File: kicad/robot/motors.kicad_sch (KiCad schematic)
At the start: 15 parts, among them J3 67996-412HLF, Q6 SN74AHC125RGYR, U8 DRV8830DRCR, U9 DRV8830DRCR

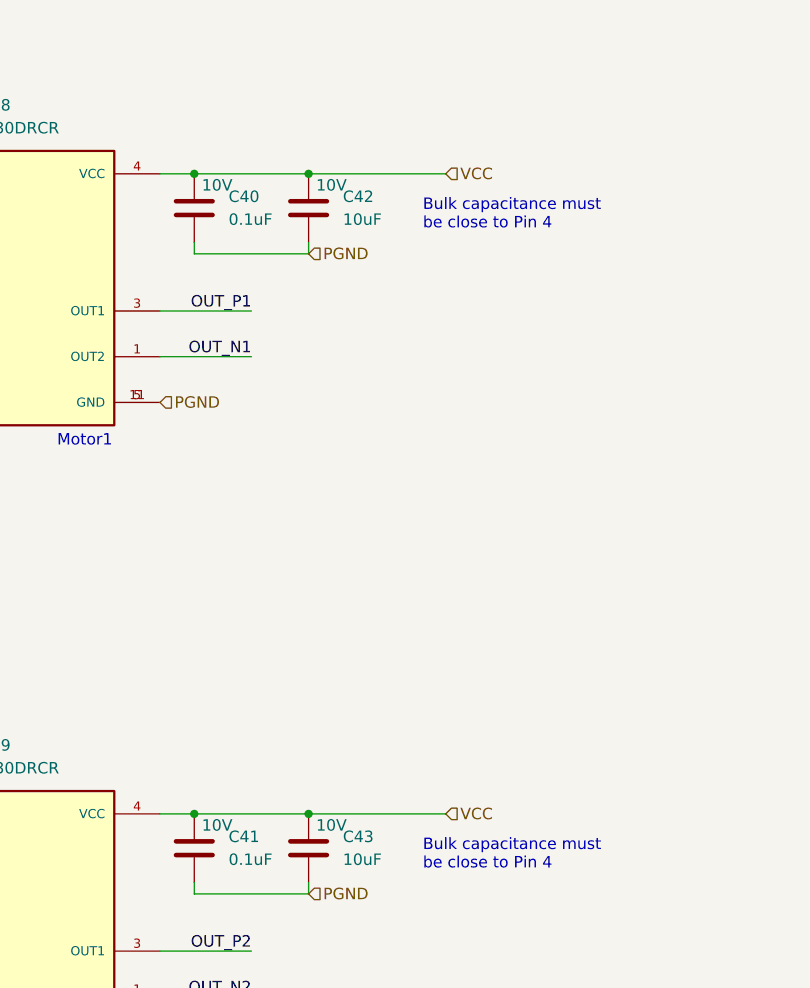
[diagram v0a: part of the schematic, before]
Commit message: Add current breaks between each section of hardware.
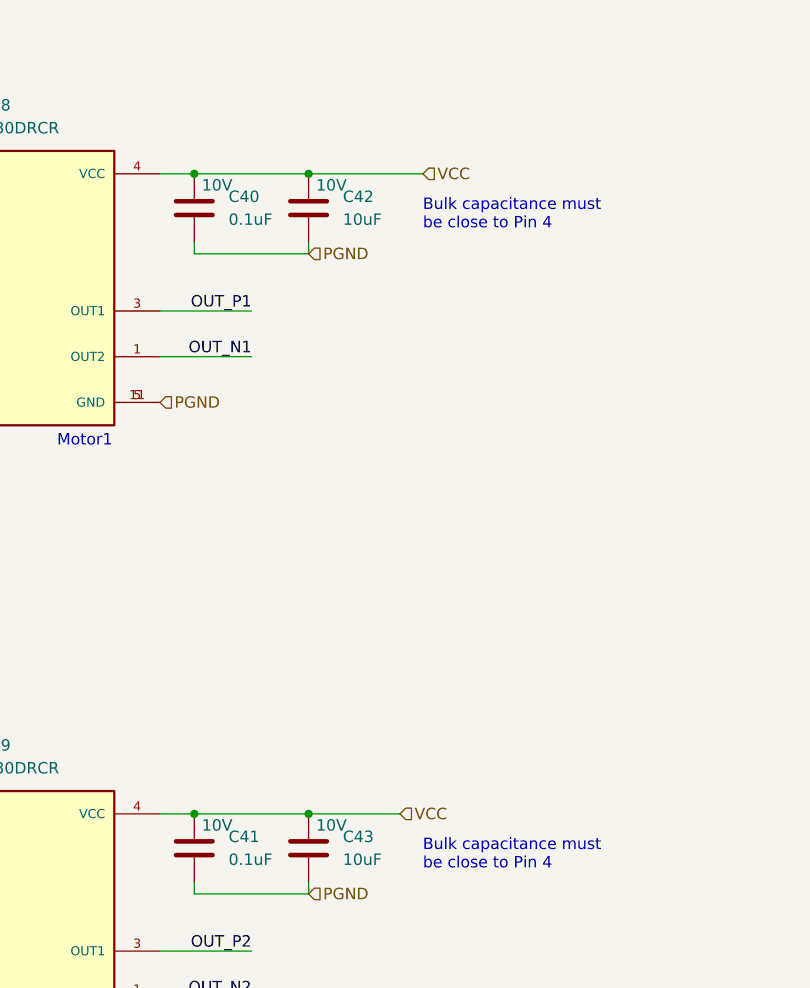
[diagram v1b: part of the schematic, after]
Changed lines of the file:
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@@
     (stroke (width 0) (type default))
   )
-  (wire (pts (xy 146.05 116.84) (xy 130.81 116.84))
+  (wire (pts (xy 140.97 116.84) (xy 130.81 116.84))
     (stroke (width 0) (type default))
   )
@@
     (stroke (width 0) (type default))
   )
-  (wire (pts (xy 146.05 45.72) (xy 130.81 45.72))
+  (wire (pts (xy 130.81 45.72) (xy 143.51 45.72))
     (stroke (width 0) (type default))
   )
@@
     (effects (font (size 1.27 1.27)) (justify left bottom))
   )
-  (hierarchical_label "VCC" (shape input) (at 146.05 45.72 0) (fields_autoplaced)
+  (hierarchical_label "VCC" (shape input) (at 143.51 45.72 0) (fields_autoplaced)
     (effects (font (size 1.27 1.27)) (justify left))
   )
@@
     (effects (font (size 1.27 1.27)) (justify right))
   )
-  (hierarchical_label "VCC" (shape input) (at 146.05 116.84 0) (fields_autoplaced)
-    (effects (font (size 1.27 1.27)) (justify left))
-  )
   (hierarchical_label "VIO" (shape input) (at 73.66 105.41 0) (fields_autoplaced)
     (effects (font (size 1.27 1.27)) (justify left))
@@
     (effects (font (size 1.27 1.27)) (justify left))
   )
+  (hierarchical_label "VCC" (shape input) (at 140.97 116.84 0) (fields_autoplaced)
+    (effects (font (size 1.27 1.27)) (justify left))
+  )

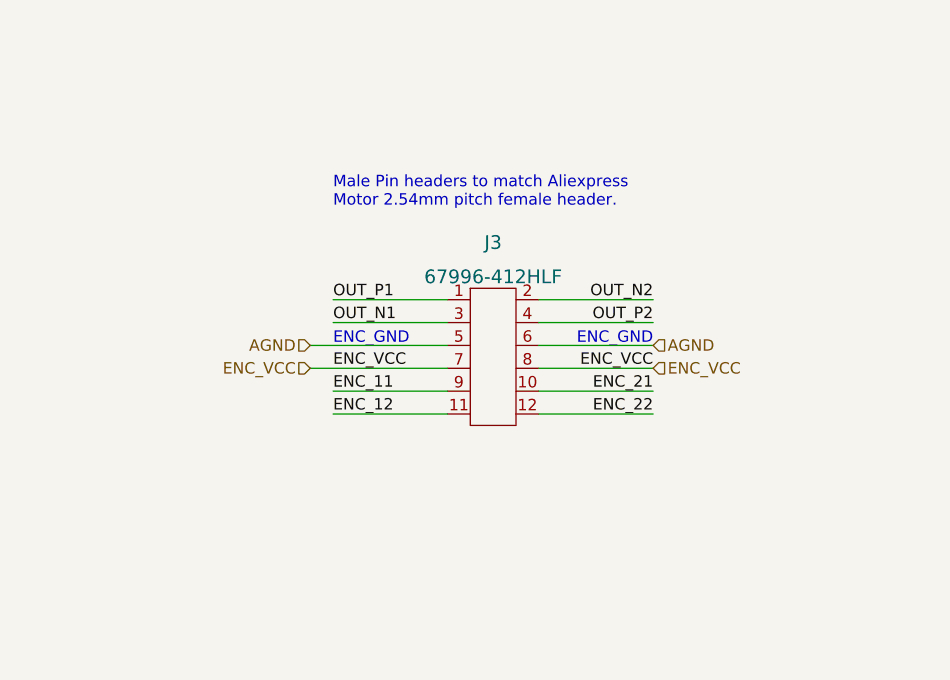
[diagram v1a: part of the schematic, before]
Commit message: Swap pins on J3 to match micromotors
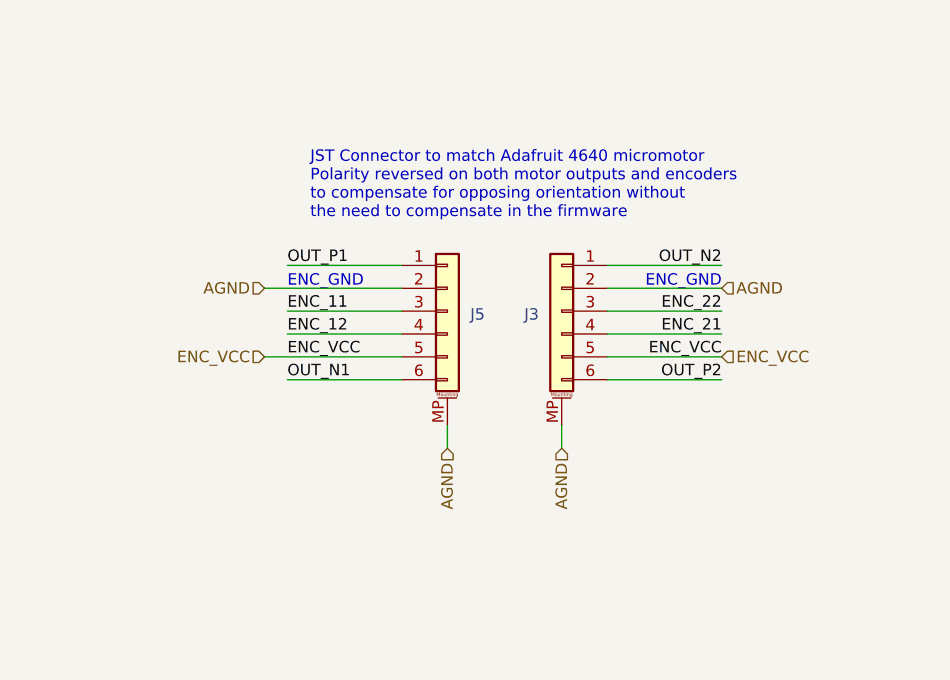
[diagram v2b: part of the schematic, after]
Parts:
- removed J3: 67996-412HLF, Connector_PinHeader_2.54mm:PinHeader_2x06_P2.54mm_Vertical, symbol dk_Rectangular-Connectors-Headers-Male-Pins:67996-412HLF
- added J3, J5: Conn_01x06_MountingPin, custom_connectors:CONN_B6B-ZR-SM4-TF_JST, symbol Connector_Generic_MountingPin:Conn_01x06_MountingPin
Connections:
- net AGND: now also J3.2 (Pin_2), J3.MP (MountPin), J5.2 (Pin_2), J5.MP (MountPin)
- net ENC_11: now also J5.3 (Pin_3)
- net ENC_12: now also J5.4 (Pin_4)
- net ENC_21: now also J3.4 (Pin_4)
- net ENC_22: now also J3.3 (Pin_3)
- net ENC_VCC: now also J3.5 (Pin_5), J5.5 (Pin_5)
- net OUT_N1: now also J5.6 (Pin_6)
- net OUT_N2: now also J3.1 (Pin_1)
- net OUT_P1: now also J5.1 (Pin_1)
- net OUT_P2: now also J3.6 (Pin_6)
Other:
- note added: "JST Connector to match Adafruit 4640 micromotor Polarity reversed on both motor outputs and encoders to compensate for opposing orientation without the need to compensate in the firmware"
- note removed: "Male Pin headers to match Aliexpress Motor 2.54mm pitch female header."

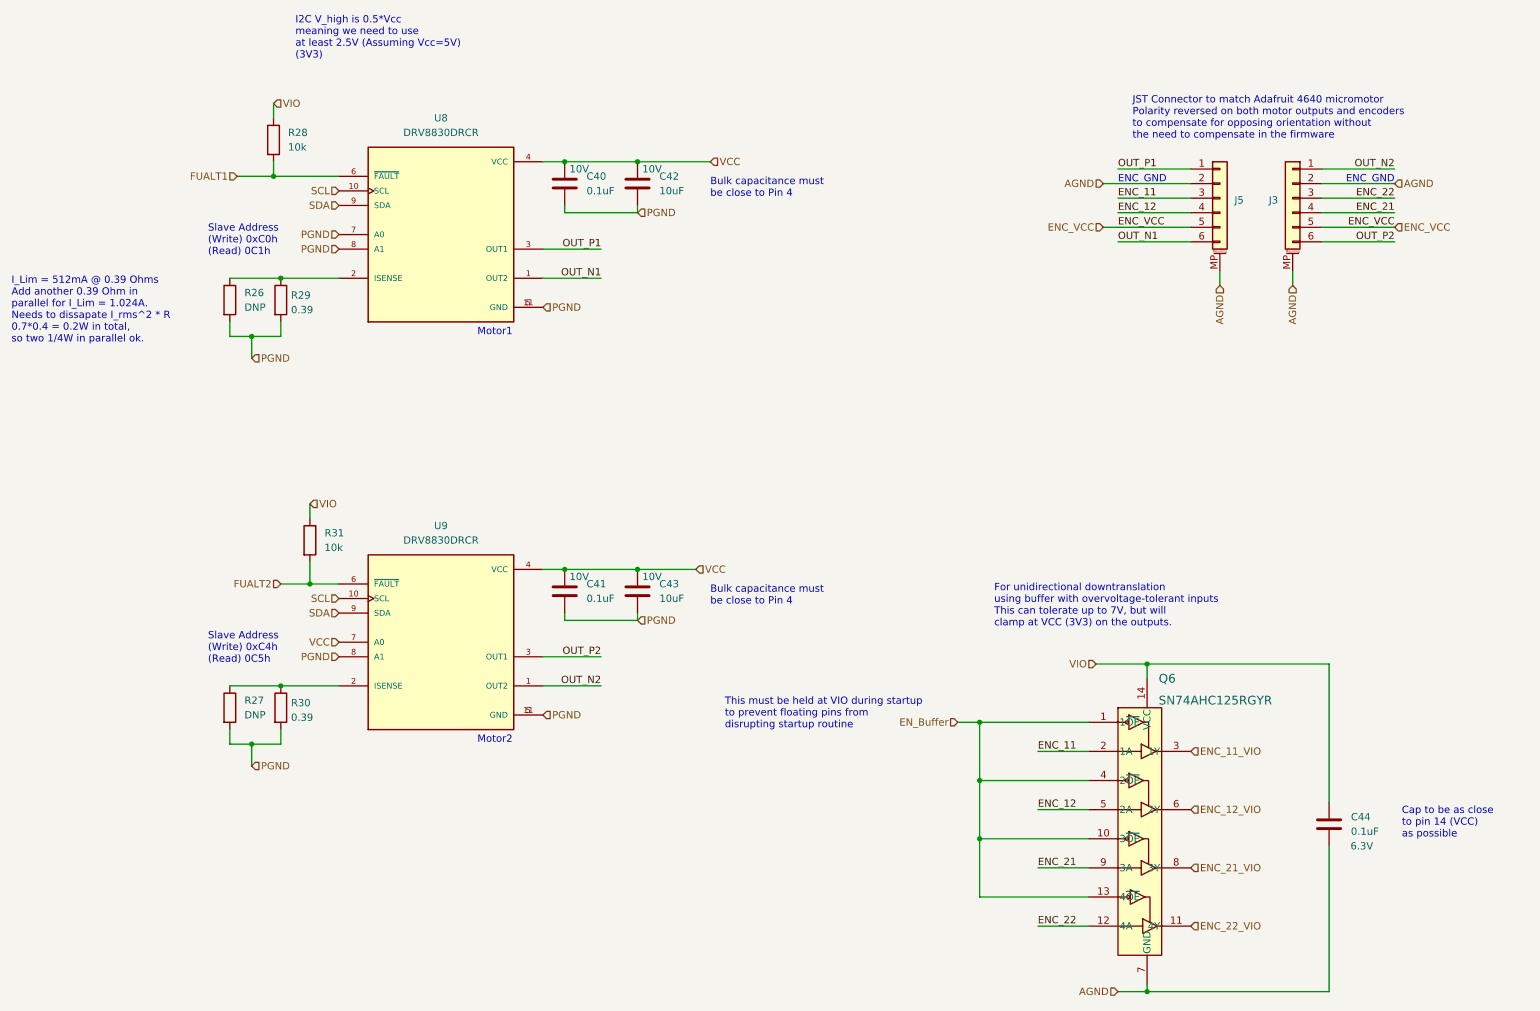
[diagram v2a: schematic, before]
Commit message: Adding DNP bulk capacitance to SYS and Vboost rails. Some populared
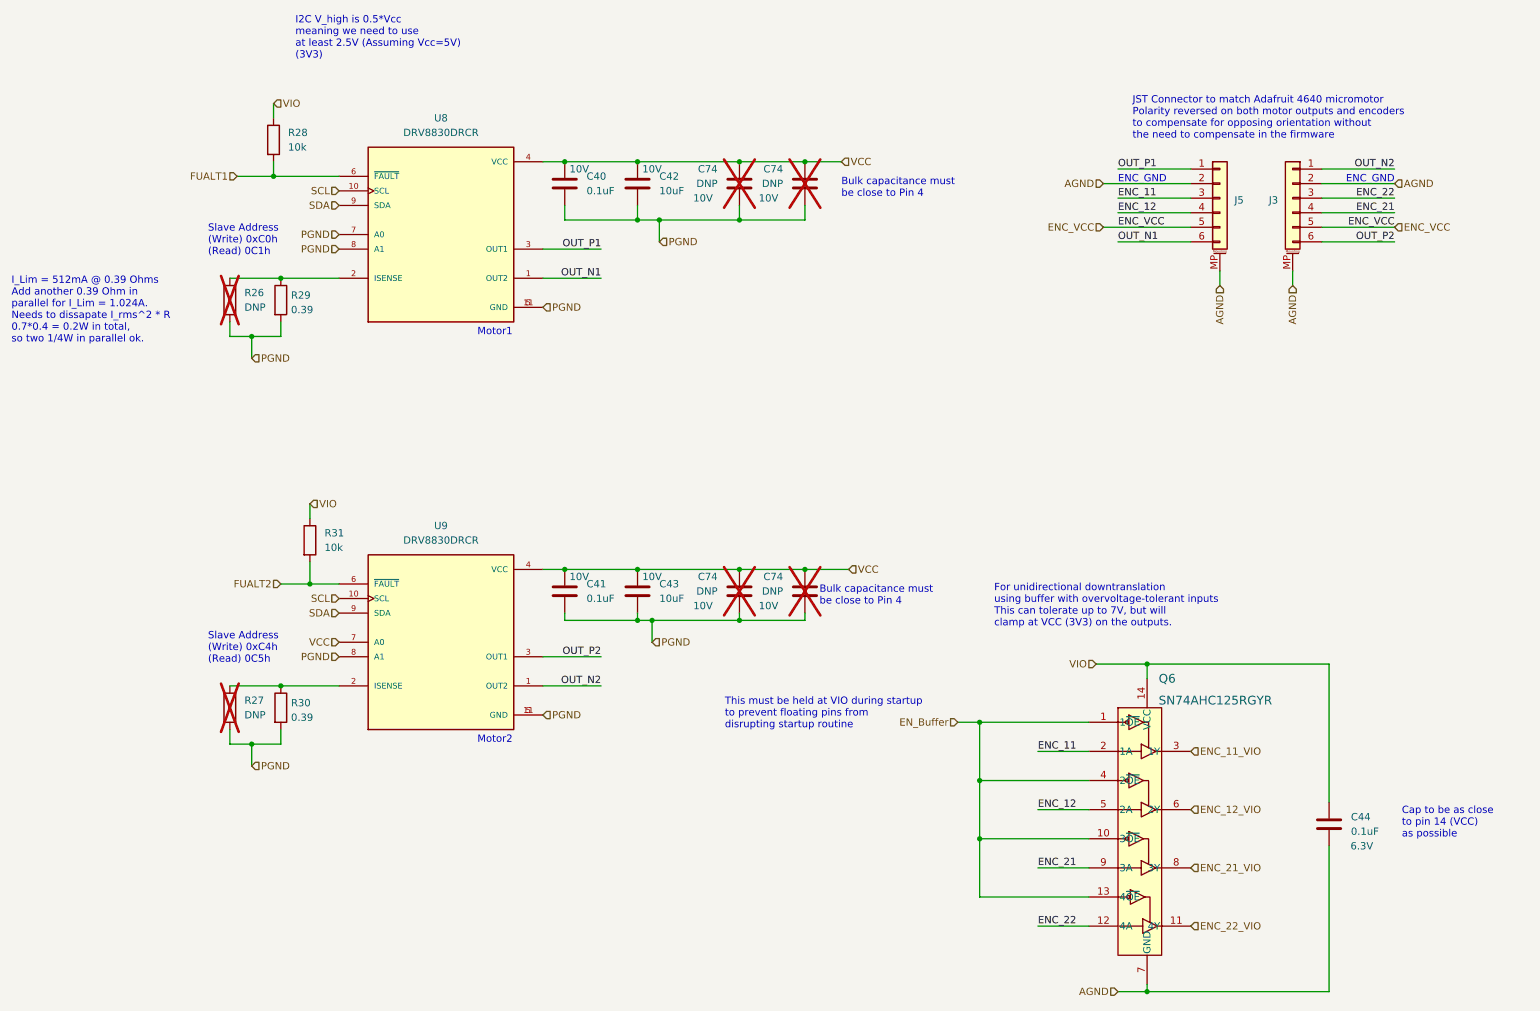
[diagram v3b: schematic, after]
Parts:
- added C74 (x4): DNP, Capacitor_SMD:C_0805_2012Metric, symbol Device:C
- R26, R27: now not fitted
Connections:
- net PGND: now also C74.2, C74.2, C74.2, C74.2
- net VCC: now also C74.1, C74.1, C74.1, C74.1

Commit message: updated all footprint fields in schematic symbols with local robot ones
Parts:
- C40, C41, C44: footprint Capacitor_SMD:C_0402_1005Metric -> robot:C_0402_1005Metric
- C42, C43: footprint Capacitor_SMD:C_0603_1608Metric -> robot:C_0603_1608Metric
- C74: footprint Capacitor_SMD:C_0805_2012Metric -> robot:C_0805_2012Metric
- J3, J5: footprint custom_connectors:CONN_B6B-ZR-SM4-TF_JST -> robot:CONN_B6B-ZR-SM4-TF_JST
- Q6: footprint Ultra_Librarian:SN74AHC125RGYR -> robot:SN74AHC125RGYR
- R26, R27, R28, R29, R30, R31: footprint Resistor_SMD:R_0603_1608Metric -> robot:R_0603_1608Metric
- U8, U9: footprint Snapeda:IC_DRV8830DRCR -> robot:IC_DRV8830DRCR
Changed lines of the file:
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@@
       (effects (font (size 1.524 1.524)) (justify left))
     )
-    (property "Footprint" "Ultra_Librarian:SN74AHC125RGYR" (at 218.44 122.174 0)
+    (property "Footprint" "robot:SN74AHC125RGYR" (at 218.44 122.174 0)
       (effects (font (size 1.524 1.524)) hide)
     )
@@
       (effects (font (size 1.27 1.27)) (justify left) hide)
     )
-    (property "Footprint" "custom_connectors:CONN_B6B-ZR-SM4-TF_JST" (at 245.11 52.07 0)
+    (property "Footprint" "robot:CONN_B6B-ZR-SM4-TF_JST" (at 245.11 52.07 0)
       (effects (font (size 1.27 1.27)) hide)
     )
@@
       (effects (font (size 1.27 1.27)) (justify left))
     )
-    (property "Footprint" "Resistor_SMD:R_0603_1608Metric" (at 57.912 140.97 90)
+    (property "Footprint" "robot:R_0603_1608Metric" (at 57.912 140.97 90)
       (effects (font (size 1.27 1.27)) hide)
     )
@@
       (effects (font (size 1.27 1.27)) (justify left))
     )
-    (property "Footprint" "Capacitor_SMD:C_0805_2012Metric" (at 159.0548 124.46 0)
+    (property "Footprint" "robot:C_0805_2012Metric" (at 159.0548 124.46 0)
       (effects (font (size 1.27 1.27)) hide)
     )
@@
       (effects (font (size 1.27 1.27)) (justify left))
     )
-    (property "Footprint" "Capacitor_SMD:C_0805_2012Metric" (at 159.0548 53.34 0)
+    (property "Footprint" "robot:C_0805_2012Metric" (at 159.0548 53.34 0)
       (effects (font (size 1.27 1.27)) hide)
     )
@@
       (effects (font (size 1.27 1.27)) (justify left) hide)
     )
-    (property "Footprint" "custom_connectors:CONN_B6B-ZR-SM4-TF_JST" (at 232.41 52.07 0)
+    (property "Footprint" "robot:CONN_B6B-ZR-SM4-TF_JST" (at 232.41 52.07 0)
       (effects (font (size 1.27 1.27)) hide)
     )
@@
       (effects (font (size 1.27 1.27)) (justify left))
     )
-    (property "Footprint" "Capacitor_SMD:C_0603_1608Metric" (at 131.7752 53.34 0)
+    (property "Footprint" "robot:C_0603_1608Metric" (at 131.7752 53.34 0)
       (effects (font (size 1.27 1.27)) hide)
     )
@@
       (effects (font (size 1.27 1.27)) (justify left))
     )
-    (property "Footprint" "Resistor_SMD:R_0603_1608Metric" (at 65.532 41.91 90)
+    (property "Footprint" "robot:R_0603_1608Metric" (at 65.532 41.91 90)
       (effects (font (size 1.27 1.27)) hide)
     )
@@
       (effects (font (size 1.27 1.27)) (justify left))
     )
-    (property "Footprint" "Capacitor_SMD:C_0402_1005Metric" (at 119.0752 53.34 0)
+    (property "Footprint" "robot:C_0402_1005Metric" (at 119.0752 53.34 0)
       (effects (font (size 1.27 1.27)) hide)
     )
@@
       (effects (font (size 1.27 1.27)) (justify left))
     )
-    (property "Footprint" "Resistor_SMD:R_0603_1608Metric" (at 57.912 69.85 90)
+    (property "Footprint" "robot:R_0603_1608Metric" (at 57.912 69.85 90)
       (effects (font (size 1.27 1.27)) hide)
     )
@@
       (effects (font (size 1.27 1.27)) (justify left))
     )
-    (property "Footprint" "Resistor_SMD:R_0603_1608Metric" (at 71.882 111.76 90)
+    (property "Footprint" "robot:R_0603_1608Metric" (at 71.882 111.76 90)
       (effects (font (size 1.27 1.27)) hide)
     )
@@
       (effects (font (size 1.27 1.27)) (justify left))
     )
-    (property "Footprint" "Resistor_SMD:R_0603_1608Metric" (at 66.802 140.97 90)
+    (property "Footprint" "robot:R_0603_1608Metric" (at 66.802 140.97 90)
       (effects (font (size 1.27 1.27)) hide)
     )
@@
       (effects (font (size 1.27 1.27)) (justify left))
     )
-    (property "Footprint" "Capacitor_SMD:C_0805_2012Metric" (at 147.6248 124.46 0)
+    (property "Footprint" "robot:C_0805_2012Metric" (at 147.6248 124.46 0)
       (effects (font (size 1.27 1.27)) hide)
     )
@@
       (effects (font (size 1.27 1.27)) (justify left))
     )
-    (property "Footprint" "Capacitor_SMD:C_0603_1608Metric" (at 131.7752 124.46 0)
+    (property "Footprint" "robot:C_0603_1608Metric" (at 131.7752 124.46 0)
       (effects (font (size 1.27 1.27)) hide)
     )
@@
       (effects (font (size 1.27 1.27)))
     )
-    (property "Footprint" "Snapeda:IC_DRV8830DRCR" (at 83.82 149.86 0)
+    (property "Footprint" "robot:IC_DRV8830DRCR" (at 83.82 149.86 0)
       (effects (font (size 1.27 1.27)) (justify left bottom) hide)
     )
@@
       (effects (font (size 1.27 1.27)) (justify left))
     )
-    (property "Footprint" "Capacitor_SMD:C_0402_1005Metric" (at 119.0752 124.46 0)
+    (property "Footprint" "robot:C_0402_1005Metric" (at 119.0752 124.46 0)
       (effects (font (size 1.27 1.27)) hide)
     )
@@
       (effects (font (size 1.27 1.27)))
     )
-    (property "Footprint" "Snapeda:IC_DRV8830DRCR" (at 83.82 78.74 0)
+    (property "Footprint" "robot:IC_DRV8830DRCR" (at 83.82 78.74 0)
       (effects (font (size 1.27 1.27)) (justify left bottom) hide)
     )
@@
       (effects (font (size 1.27 1.27)) (justify left))
     )
-    (property "Footprint" "Capacitor_SMD:C_0402_1005Metric" (at 252.4252 165.1 0)
+    (property "Footprint" "robot:C_0402_1005Metric" (at 252.4252 165.1 0)
       (effects (font (size 1.27 1.27)) hide)
     )
@@
       (effects (font (size 1.27 1.27)) (justify left))
     )
-    (property "Footprint" "Resistor_SMD:R_0603_1608Metric" (at 66.802 69.85 90)
+    (property "Footprint" "robot:R_0603_1608Metric" (at 66.802 69.85 90)
       (effects (font (size 1.27 1.27)) hide)
     )
@@
       (effects (font (size 1.27 1.27)) (justify left))
     )
-    (property "Footprint" "Capacitor_SMD:C_0805_2012Metric" (at 147.6248 53.34 0)
-      (effects (font (size 1.27 1.27)) hide)
-    )
+    (property "Footprint" "robot:C_0805_2012Metric" (at 147.6248 53.34 0)
+      (effects (font (size 1.27 1.27)) hide)
+    )
